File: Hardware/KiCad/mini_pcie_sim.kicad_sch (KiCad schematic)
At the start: 9 parts, among them J10 2041262-1, J9 SIM8066-6-1-14-01-A, U5 EMIF03-SIM02M8

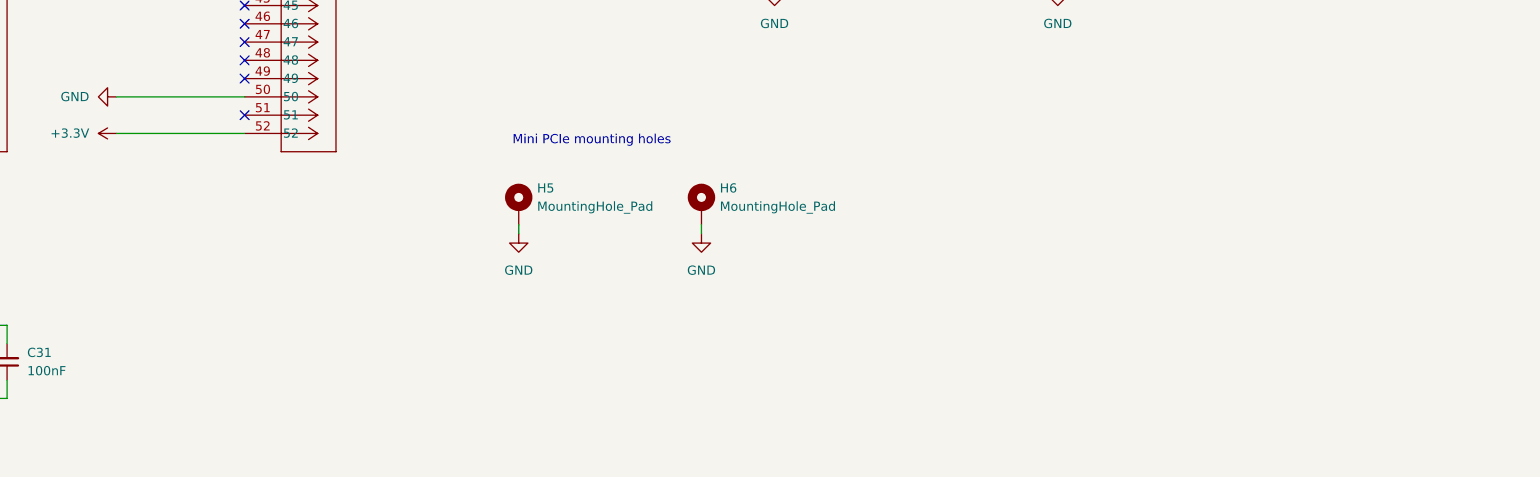
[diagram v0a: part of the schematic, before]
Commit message: Add switches for cpu reset and watchdog reset Add swtich for WWAN wirless disable Fix USB2422 VBUS-DET and NON_REM strap pins
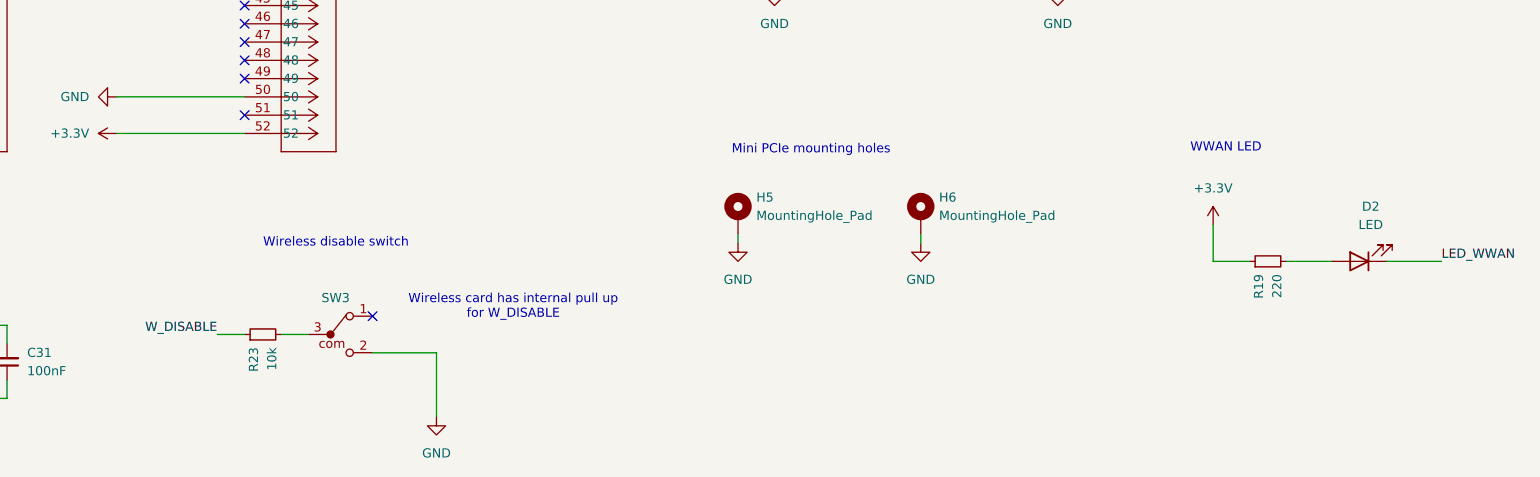
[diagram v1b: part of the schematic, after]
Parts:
- added D2: LED, LED_SMD:LED_0805_2012Metric, symbol Device:LED
- added R19: 220, Resistor_SMD:R_0402_1005Metric, symbol Device:R_Small
- added R23: 10k, Resistor_SMD:R_0402_1005Metric, symbol Device:R_Small
- added SW3: 450405020524, WS-SLSU:SW_Wurth_WS-SLSU_450405020524, symbol WS-SLSU:450405020524
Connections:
- net +3.3V: now also R19.1
- net GND: now also SW3.2
- net LED_WWAN: now also D2.1 (K)
- net W_DISABLE: now also R23.1
- new net: R23.2, SW3.3
- new net: D2.2 (A), R19.2
- no-connect marks 21 -> 22
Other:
- note added: "WWAN LED"
- note added: "Wireless card has internal pull up for W_DISABLE"
- note added: "Wireless disable switch"
- moved on the sheet: H5, H6

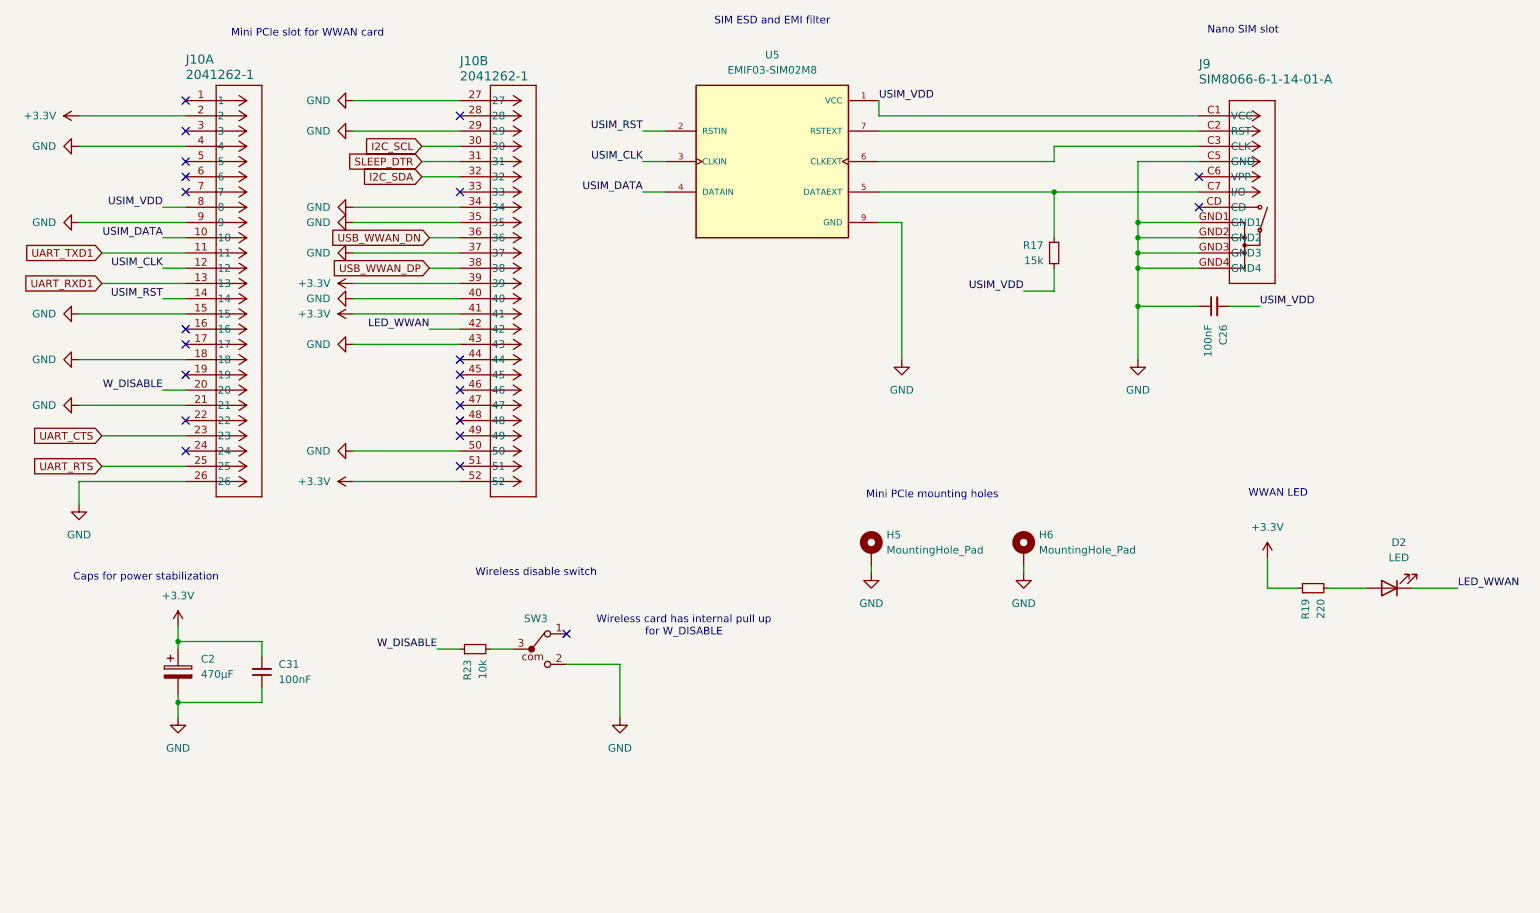
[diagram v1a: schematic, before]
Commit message: Fix footprints for Mini PCIe and switches (set pads for mounting and case to GND) Set PCB to 4 layer with 0.5 OZ (0,017mm) copper on the inner layers Start sorting the footprints on the PCB TO-DO: check footprints of Y1 and Y2, they seem way too large
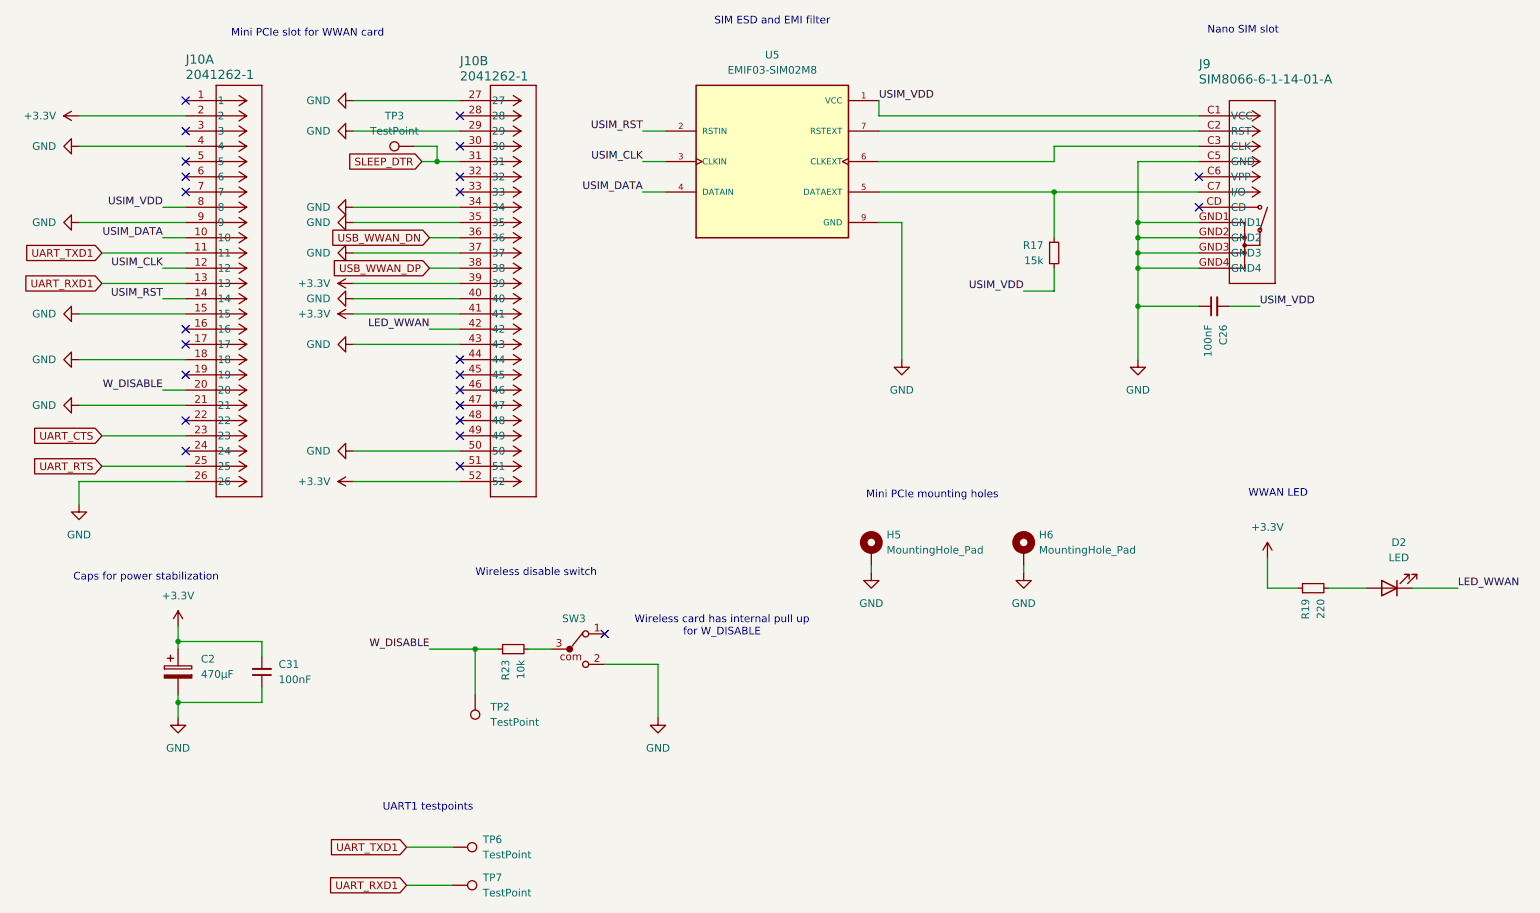
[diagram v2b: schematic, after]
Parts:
- added TP2, TP3, TP6, TP7: TestPoint, TestPoint:TestPoint_Pad_D2.0mm, symbol Connector:TestPoint
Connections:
- net SLEEP_DTR: now also TP3.1
- net UART_RXD1: now also TP7.1
- net UART_TXD1: now also TP6.1
- net W_DISABLE: now also TP2.1
- net I2C_SCL: no longer names the net of J10.30
- net I2C_SDA: no longer names the net of J10.32
- no-connect marks 22 -> 24
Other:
- note added: "UART1 testpoints"
- moved on the sheet: R23, SW3
